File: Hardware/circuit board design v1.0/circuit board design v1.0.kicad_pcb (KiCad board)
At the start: 4 copper layers, 31 x 80 mm, 34 parts, among them IC1 BMI088, J1 Conn_01x06_Male, J3 105017-0001, Q1 2N7002-7-F, U1 STM32F446RETx, U2 W25Q64JVSS, U4 BME280, U5 STF202-22T1G, U6 MAX40203_SOT23, U7 NCP161ASN180T1G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

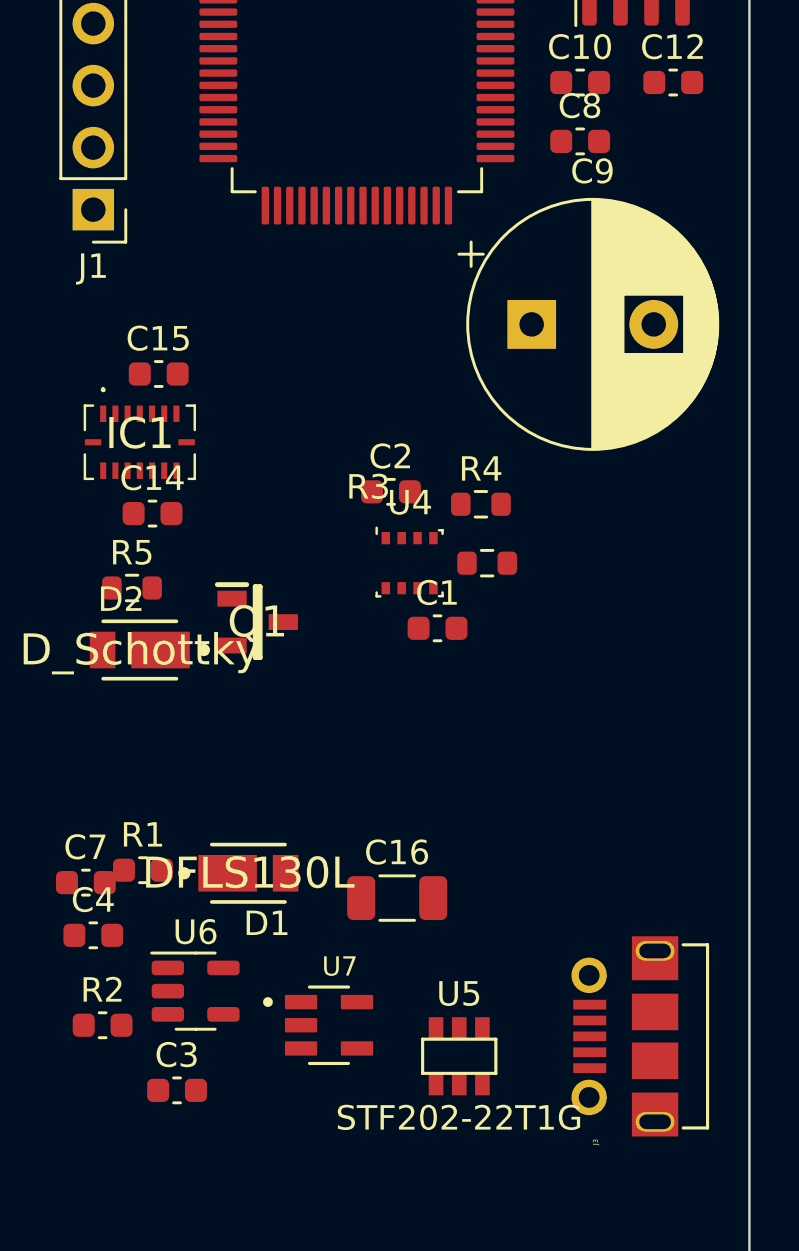
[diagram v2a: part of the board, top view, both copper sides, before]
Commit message: Added spi connection for radio
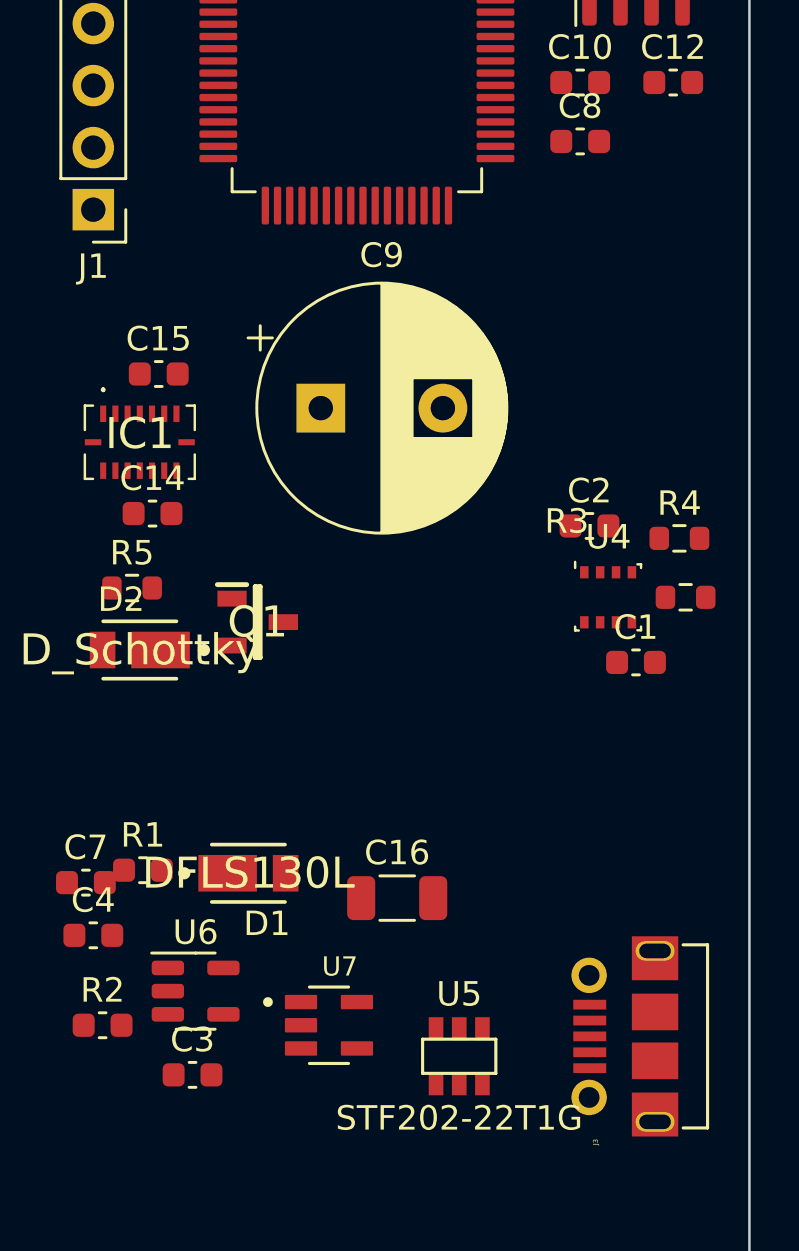
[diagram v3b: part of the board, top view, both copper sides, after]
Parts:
- moved C9 9.29 mm to (33.4, 65.4)
- moved C1 8.25 mm to (46.4, 75.8)
- moved R3 8.25 mm to (48.4, 73.2)
- moved R4 8.25 mm to (48.1, 70.7)
- moved U4 8.25 mm to (45.2, 73.2)
- moved C2 8.25 mm to (44.5, 70.2)
- moved C3 0.90 mm to (28.2, 92.7)
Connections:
- U1 pad 21: unconnected-(U1-Pad21) -> /MCU/SPI1_SCK
- U1 pad 22: unconnected-(U1-Pad22) -> /MCU/SPI1_MISO
- U1 pad 23: unconnected-(U1-Pad23) -> /MCU/SPI1_MOSI
- U1 pad 24: unconnected-(U1-Pad24) -> /MCU/Radio_Enable
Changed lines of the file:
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@@
 (kicad_pcb (version 20211014) (generator pcbnew)
   (general
-    (thickness 4.69)
+    (thickness 1.6062)
   )
   (paper "A4")
@@
       (layer "F.Mask" (type "Top Solder Mask") (thickness 0.01))
       (layer "F.Cu" (type "copper") (thickness 0.035))
-      (layer "dielectric 1" (type "core") (thickness 1.51) (material "FR4") (epsilon_r 4.5) (loss_tangent 0.02))
-      (layer "In1.Cu" (type "copper") (thickness 0.035))
-      (layer "dielectric 2" (type "prepreg") (thickness 1.51) (material "FR4") (epsilon_r 4.5) (loss_tangent 0.02))
-      (layer "In2.Cu" (type "copper") (thickness 0.035))
-      (layer "dielectric 3" (type "core") (thickness 1.51) (material "FR4") (epsilon_r 4.5) (loss_tangent 0.02))
+      (layer "dielectric 1" (type "prepreg") (thickness 0.2104) (material "FR4") (epsilon_r 4.5) (loss_tangent 0.02))
+      (layer "In1.Cu" (type "copper") (thickness 0.0152))
+      (layer "dielectric 2" (type "core") (thickness 1.065) (material "FR4") (epsilon_r 4.5) (loss_tangent 0.02))
+      (layer "In2.Cu" (type "copper") (thickness 0.0152))
+      (layer "dielectric 3" (type "prepreg") (thickness 0.2104) (material "FR4") (epsilon_r 4.5) (loss_tangent 0.02))
       (layer "B.Cu" (type "copper") (thickness 0.035))
       (layer "B.Mask" (type "Bottom Solder Mask") (thickness 0.01))
@@
   (net 18 "unconnected-(IC1-Pad5)")
   (net 19 "unconnected-(U1-Pad20)")
-  (net 20 "unconnected-(U1-Pad21)")
-  (net 21 "unconnected-(U1-Pad22)")
-  (net 22 "unconnected-(U1-Pad23)")
-  (net 23 "unconnected-(U1-Pad24)")
+  (net 20 "/MCU/SPI1_SCK")
+  (net 21 "/MCU/SPI1_MISO")
+  (net 22 "/MCU/SPI1_MOSI")
+  (net 23 "/MCU/Radio_Enable")
   (net 24 "unconnected-(U1-Pad25)")
   (net 25 "unconnected-(U1-Pad26)")
@@
   (net 81 "/MCU/buzzer_gate")
   (footprint "Resistor_SMD:R_0603_1608Metric" (layer "F.Cu")
-    (at 40.005 69.342)
+    (at 48.133 70.739)
     (descr "Resistor SMD 0603 (1608 Metric), square (rectangular) end terminal, IPC_7351 nominal, (Body size source: IPC-SM-782 page 72, https://www.pcb-3d.com/wordpress/wp-content/uploads/ipc-sm-782a_amendment_1_and_2.pdf), generated with kicad-footprint-generator")
     (tags "resistor")
@@
       (effects (font (size 0.200353 0.200353) (thickness 0.15)))
     )
+    (fp_line (start -3.75 2.15) (end 3.75 2.15) (layer "F.SilkS") (width 0.127))
+    (fp_line (start 3.75 1.15) (end 3.75 2.15) (layer "F.SilkS") (width 0.127))
     (fp_line (start -3.75 1.15) (end -3.75 2.15) (layer "F.SilkS") (width 0.127))
-    (fp_line (start 3.75 1.15) (end 3.75 2.15) (layer "F.SilkS") (width 0.127))
-    (fp_line (start -3.75 2.15) (end 3.75 2.15) (layer "F.SilkS") (width 0.127))
-    (fp_line (start 4 -3.6) (end -4 -3.6) (layer "F.CrtYd") (width 0.127))
-    (fp_line (start -4.4 1.7) (end 4.4 1.7) (layer "F.CrtYd") (width 0.127))
-    (fp_line (start -4 -3.6) (end -4 -1.3) (layer "F.CrtYd") (width 0.127))
     (fp_line (start 4.4 1.7) (end 4.4 -1.3) (layer "F.CrtYd") (width 0.127))
-    (fp_line (start -4 -1.3) (end -4.4 -1.3) (layer "F.CrtYd") (width 0.127))
     (fp_line (start -4.4 -1.3) (end -4.4 1.7) (layer "F.CrtYd") (width 0.127))
     (fp_line (start 4.4 -1.3) (end 4 -1.3) (layer "F.CrtYd") (width 0.127))
+    (fp_line (start -4.4 1.7) (end 4.4 1.7) (layer "F.CrtYd") (width 0.127))
+    (fp_line (start -4 -1.3) (end -4.4 -1.3) (layer "F.CrtYd") (width 0.127))
+    (fp_line (start 4 -3.6) (end -4 -3.6) (layer "F.CrtYd") (width 0.127))
+    (fp_line (start -4 -3.6) (end -4 -1.3) (layer "F.CrtYd") (width 0.127))
     (fp_line (start 4 -1.3) (end 4 -3.6) (layer "F.CrtYd") (width 0.127))
     (fp_line (start 4.05 2.55) (end 4.05 2.8) (layer "B.Fab") (width 0.127))
+    (fp_arc (start 4.05 2.8) (mid 3.656711 2.575094) (end 3.5 2.15) (layer "B.Fab") (width 0.127))
     (fp_arc (start 4.05 2.55) (mid 3.824711 2.406466) (end 3.75 2.15) (layer "B.Fab") (width 0.127))
-    (fp_arc (start 4.05 2.8) (mid 3.656711 2.575094) (end 3.5 2.15) (layer "B.Fab") (width 0.127))
-    (fp_line (start 3.75 -2.85) (end -3.75 -2.85) (layer "F.Fab") (width 0.127))
-    (fp_line (start -3.75 -2.85) (end -3.75 2.15) (layer "F.Fab") (width 0.127))
     (fp_line (start -4.7 1.45) (end 4.85 1.45) (layer "F.Fab") (width 0.127))
     (fp_line (start 3.75 2.15) (end 3.75 -2.85) (layer "F.Fab") (width 0.127))
+    (fp_line (start -3.75 -2.85) (end -3.75 2.15) (layer "F.Fab") (width 0.127))
     (fp_line (start -4.05 2.55) (end -4.05 2.8) (layer "F.Fab") (width 0.127))
+    (fp_line (start 3.75 -2.85) (end -3.75 -2.85) (layer "F.Fab") (width 0.127))
+    (fp_arc (start -3.75 2.15) (mid -3.824721 2.406459) (end -4.05 2.55) (layer "F.Fab") (width 0.127))
     (fp_arc (start -3.5 2.15) (mid -3.65671 2.575091) (end -4.05 2.8) (layer "F.Fab") (width 0.127))
-    (fp_arc (start -3.75 2.15) (mid -3.824721 2.406459) (end -4.05 2.55) (layer "F.Fab") (width 0.127))
     (pad "1" smd rect (at -1.3 -2.675 90) (size 0.4 1.35) (layers "F.Cu" "F.Paste" "F.Mask")
       (net 61 "VBUS") (pinfunction "VDD") (pintype "power_in"))
@@
   )
   (footprint "Capacitor_SMD:C_0603_1608Metric" (layer "F.Cu")
-    (at 38.227 74.422)
+    (at 46.355 75.819)
     (descr "Capacitor SMD 0603 (1608 Metric), square (rectangular) end terminal, IPC_7351 nominal, (Body size source: IPC-SM-782 page 76, https://www.pcb-3d.com/wordpress/wp-content/uploads/ipc-sm-782a_amendment_1_and_2.pdf), generated with kicad-footprint-generator")
     (tags "capacitor")
@@
   )
   (footprint "Capacitor_THT:CP_Radial_D10.0mm_P5.00mm" (layer "F.Cu")
-    (at 42.082323 61.976)
+    (at 33.446323 65.405)
     (descr "CP, Radial series, Radial, pin pitch=5.00mm, , diameter=10mm, Electrolytic Capacitor")
     (tags "CP Radial series Radial pin pitch 5.00mm  diameter 10mm Electrolytic Capacitor")
@@
   )
   (footprint "Capacitor_SMD:C_0603_1608Metric" (layer "F.Cu")
-    (at 27.559 93.345)
+    (at 28.194 92.71)
     (descr "Capacitor SMD 0603 (1608 Metric), square (rectangular) end terminal, IPC_7351 nominal, (Body size source: IPC-SM-782 page 76, https://www.pcb-3d.com/wordpress/wp-content/uploads/ipc-sm-782a_amendment_1_and_2.pdf), generated with kicad-footprint-generator")
     (tags "capacitor")
@@
   )
   (footprint "Package_LGA:Bosch_LGA-8_2.5x2.5mm_P0.65mm_ClockwisePinNumbering" (layer "F.Cu")
-    (at 37.084 71.755)
+    (at 45.212 73.152)
     (descr "LGA-8")
     (tags "lga land grid array")
@@
   )
   (footprint "Resistor_SMD:R_0603_1608Metric" (layer "F.Cu")
-    (at 40.259 71.755)
+    (at 48.387 73.152)
     (descr "Resistor SMD 0603 (1608 Metric), square (rectangular) end terminal, IPC_7351 nominal, (Body size source: IPC-SM-782 page 72, https://www.pcb-3d.com/wordpress/wp-content/uploads/ipc-sm-782a_amendment_1_and_2.pdf), generated with kicad-footprint-generator")
     (tags "resistor")
@@
   )
   (footprint "Capacitor_SMD:C_0603_1608Metric" (layer "F.Cu")
-    (at 36.322 68.834)
+    (at 44.45 70.231)
     (descr "Capacitor SMD 0603 (1608 Metric), square (rectangular) end terminal, IPC_7351 nominal, (Body size source: IPC-SM-782 page 76, https://www.pcb-3d.com/wordpress/wp-content/uploads/ipc-sm-782a_amendment_1_and_2.pdf), generated with kicad-footprint-generator")
     (tags "capacitor")
@@
       (net 19 "unconnected-(U1-Pad20)") (pinfunction "PA4") (pintype "bidirectional+no_connect"))
     (pad "21" smd roundrect (at -1.75 5.675) (size 0.3 1.55) (layers "F.Cu" "F.Paste" "F.Mask") (roundrect_rratio 0.25)
-      (net 20 "unconnected-(U1-Pad21)") (pinfunction "PA5") (pintype "bidirectional+no_connect"))
+      (net 20 "/MCU/SPI1_SCK") (pinfunction "PA5") (pintype "bidirectional"))
     (pad "22" smd roundrect (at -1.25 5.675) (size 0.3 1.55) (layers "F.Cu" "F.Paste" "F.Mask") (roundrect_rratio 0.25)
-      (net 21 "unconnected-(U1-Pad22)") (pinfunction "PA6") (pintype "bidirectional+no_connect"))
+      (net 21 "/MCU/SPI1_MISO") (pinfunction "PA6") (pintype "bidirectional"))
     (pad "23" smd roundrect (at -0.75 5.675) (size 0.3 1.55) (layers "F.Cu" "F.Paste" "F.Mask") (roundrect_rratio 0.25)
-      (net 22 "unconnected-(U1-Pad23)") (pinfunction "PA7") (pintype "bidirectional+no_connect"))
+      (net 22 "/MCU/SPI1_MOSI") (pinfunction "PA7") (pintype "bidirectional"))
     (pad "24" smd roundrect (at -0.25 5.675) (size 0.3 1.55) (layers "F.Cu" "F.Paste" "F.Mask") (roundrect_rratio 0.25)
-      (net 23 "unconnected-(U1-Pad24)") (pinfunction "PC4") (pintype "bidirectional+no_connect"))
+      (net 23 "/MCU/Radio_Enable") (pinfunction "PC4") (pintype "bidirectional"))
     (pad "25" smd roundrect (at 0.25 5.675) (size 0.3 1.55) (layers "F.Cu" "F.Paste" "F.Mask") (roundrect_rratio 0.25)
       (net 24 "unconnected-(U1-Pad25)") (pinfunction "PC5") (pintype "bidirectional+no_connect"))

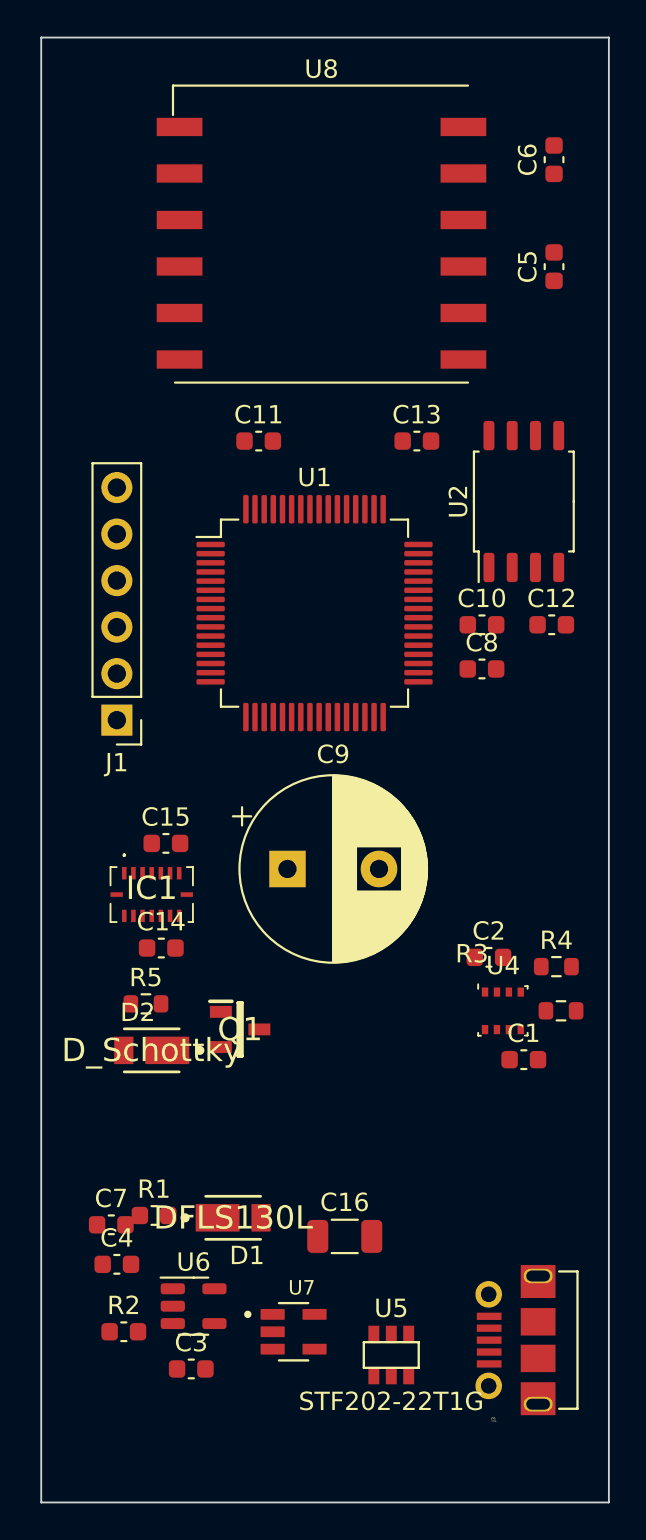
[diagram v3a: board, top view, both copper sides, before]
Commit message: Placed components but not connected yet
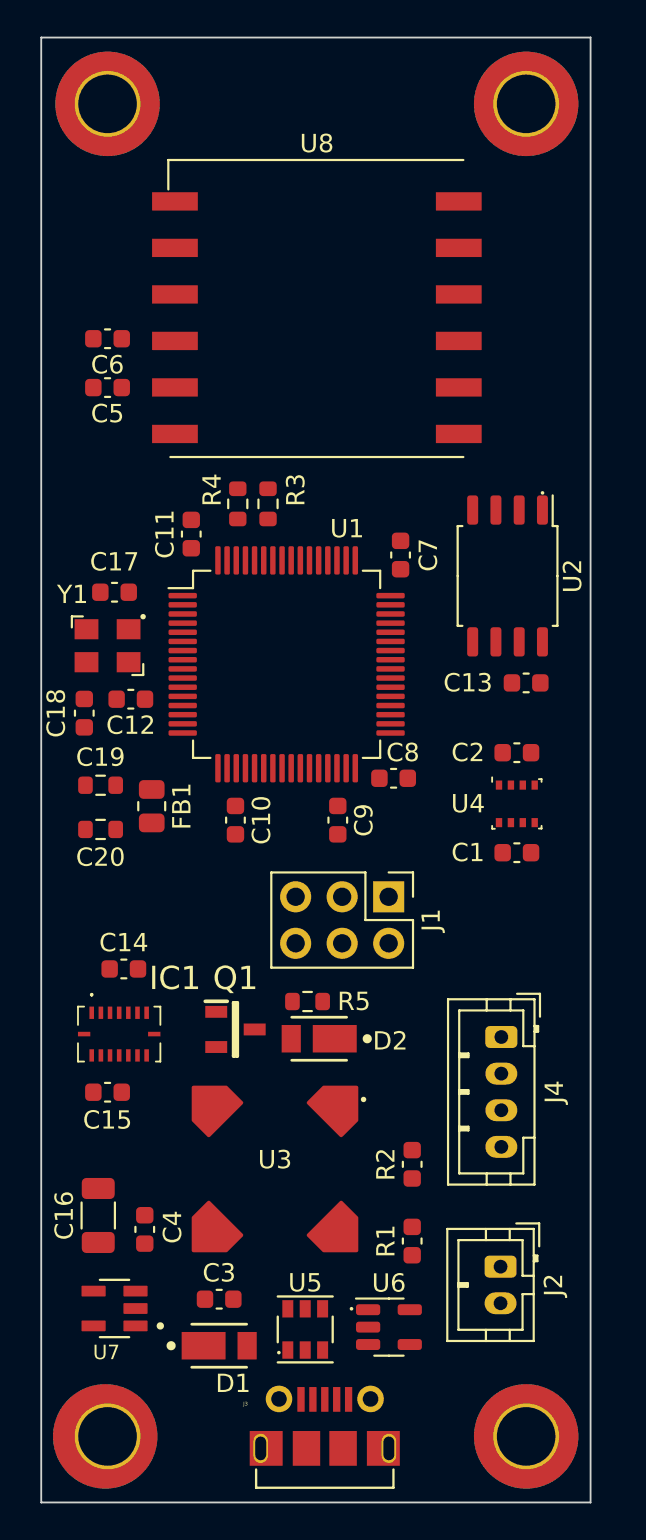
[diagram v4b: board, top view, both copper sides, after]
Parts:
- added C17: 8pF, Capacitor_SMD:C_0603_1608Metric, F.Cu at (24.0, 50.3)
- added C18: 8pF, Capacitor_SMD:C_0603_1608Metric, F.Cu at (22.4, 56.9)
- added C19: 1uF, Resistor_SMD:R_0603_1608Metric, F.Cu at (23.2, 60.8)
- added C20: 1uF, Resistor_SMD:R_0603_1608Metric, F.Cu at (23.2, 63.2)
- added FB1: 120R@100MHz, Resistor_SMD:R_0805_2012Metric, F.Cu at (26.0, 62.0)
- added H1: MountingHole_Pad, MountingHole:MountingHole_3.2mm_M3_ISO7380_Pad_TopBottom, F.Cu at (23.5, 96.4)
- added H2: MountingHole_Pad, MountingHole:MountingHole_3.2mm_M3_ISO7380_Pad_TopBottom, F.Cu at (46.5, 23.6)
- added H3: MountingHole_Pad, MountingHole:MountingHole_3.2mm_M3_ISO7380_Pad_TopBottom, F.Cu at (23.6, 23.6)
- added H4: MountingHole_Pad, MountingHole:MountingHole_3.2mm_M3_ISO7380_Pad_TopBottom, F.Cu at (46.5, 96.4)
- added J2: Conn_01x02, Connector_JST:JST_PH_B2B-PH-K_1x02_P2.00mm_Vertical, F.Cu at (45.1, 87.1)
- added J4: Conn_01x04, Connector_JST:JST_PH_B4B-PH-K_1x04_P2.00mm_Vertical, F.Cu at (45.1, 74.6)
- added U3: SDR08540M3-01, Components:SDR08540M3-01 Buzzer, F.Cu at (32.8, 81.8)
- added Y1: Crystal_GND24, Components:ECS-80-8-33Q-ADS-TR3 Crystal, F.Cu at (23.6, 53.2)
- C1, C2: value 100n -> 100nF
- C14, C15: value C_Small -> 100nF
- C3, C4: value C_Small -> 1uF
- C9: footprint Capacitor_THT:CP_Radial_D10.0mm_P5.00mm -> Capacitor_SMD:C_0603_1608Metric
- J1: footprint Connector_PinHeader_2.54mm:PinHeader_1x06_P2.54mm_Vertical -> Connector_PinHeader_2.54mm:PinHeader_2x03_P2.54mm_Vertical
- R1, R2: value R -> 100k
- moved C7 39.8 mm to (39.6, 48.3), turned to 90 degrees
- moved R3 32.0 mm to (32.4, 45.5), turned to 90 degrees
- moved R4 30.7 mm to (30.7, 45.5), turned to 90 degrees
- moved C6 26.3 mm to (23.6, 36.4), turned to 180 degrees
- moved C5 25.3 mm to (23.6, 39.1), turned to 180 degrees
- moved C12 23.3 mm to (24.9, 56.1), turned to 180 degrees
- moved R2 18.2 mm to (40.3, 81.5), turned to 90 degrees
- moved J1 17.7 mm to (39.0, 66.9), turned to -90 degrees
- moved C10 17.2 mm to (30.6, 62.7), turned to -90 degrees
- moved C13 14.5 mm to (46.5, 55.2), turned to 180 degrees
- moved R1 14.2 mm to (40.3, 85.7), turned to 90 degrees
- moved C15 14.0 mm to (23.6, 77.6)
- moved C16 13.5 mm to (23.1, 84.3), turned to 90 degrees
- moved J3 13.1 mm to (35.5, 97.0), turned to 0 degrees
- moved U4 11.3 mm to (46.0, 61.8)
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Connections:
- IC1 pad 9: /MCU/SCL -> /MCU/SDA
- R1 pad 2: /Power/PWR_BVOLTS -> /MCU/PWR_BVOLTS
- R2 pad 1: /Power/PWR_BVOLTS -> /MCU/PWR_BVOLTS
- R3 pad 1: +3.3V -> /MCU/SDA
- R3 pad 2: /MCU/SCL -> +3.3V
- U1 pad 14: /GPS/rx_gps -> unconnected-(U1-Pad14)
- U1 pad 15: /GPS/tx_gps -> unconnected-(U1-Pad15)
- U1 pad 25: unconnected-(U1-Pad25) -> /MCU/PWR_BVOLTS
- U1 pad 53: unconnected-(U1-Pad53) -> /GPS/rx_gps
- U1 pad 54: unconnected-(U1-Pad54) -> /GPS/tx_gps
- U1 pad 59: /MCU/SCL -> /MCU/SDA
- U4 pad 3: /MCU/SCL -> /MCU/SDA
- U4 pad 6: +3.3V -> unconnected-(U4-Pad6)
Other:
- board size 31 x 80 mm -> 30 x 80 mm

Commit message: Finished routing
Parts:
- J2: footprint Connector_JST:JST_PH_B2B-PH-K_1x02_P2.00mm_Vertical -> Components:JST_PH_B2B-PH-K_1x02_P2.00mm_Vertical
- J4: footprint Connector_JST:JST_PH_B4B-PH-K_1x04_P2.00mm_Vertical -> Components:JST_PH_B4B-PH-K_1x04_P2.00mm_Vertical
- U1: footprint Package_QFP:LQFP-64_10x10mm_P0.5mm -> Components:LQFP-64_10x10mm_P0.5mm
- U2: footprint Package_SO:SOIC-8_5.23x5.23mm_P1.27mm -> Components:W25Q64JVSSIQ
- moved J1 4.41 mm to (41.9, 70.2), turned to 180 degrees
- moved C8 3.24 mm to (36.8, 62.6), turned to -90 degrees
- moved C7 1.17 mm to (40.4, 49.1), turned to 0 degrees
- moved C9 1.02 mm to (35.2, 62.6)
- moved U5 0.92 mm to (34.2, 89.7), turned to 180 degrees
- moved J3 0.51 mm to (35.5, 96.5)
- turned C2 to 180 degrees
- turned C20 to 180 degrees
- turned U6 to 180 degrees
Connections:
- U1 pad 25: /MCU/PWR_BVOLTS -> unconnected-(U1-Pad25)
- U1 pad 27: unconnected-(U1-Pad27) -> /MCU/PWR_BVOLTS
- U3 pad 2: GND -> Net-(D2-Pad2)
- U3 pad 3: GND -> Net-(D2-Pad2)
- U3 pad 4: GND -> Net-(D2-Pad2)
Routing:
- net GND: track 0.00 -> 120.9 mm, vias 0 -> 34
- net +3.3V: track 0.00 -> 77.7 mm, vias 0 -> 22
- net /MCU/SDA: track 0.00 -> 57.0 mm, vias 0 -> 3
- net /MCU/SCL: track 0.00 -> 55.7 mm, vias 0 -> 3
- net +3.3VA: track 0.00 -> 44.3 mm, vias 0 -> 4
- net /MCU/usb_dp: track 0.00 -> 42.7 mm, vias 0 -> 2
- net /MCU/usb_dm: track 0.00 -> 41.8 mm, vias 0 -> 2
- net /MCU/PWR_BVOLTS: track 0.00 -> 33.3 mm, vias 0 -> 2
- net Net-(D2-Pad2): track 0.00 -> 27.0 mm
- net /MCU/SPI1_SCK: track 0.00 -> 26.3 mm
- net /MCU/SPI1_MISO: track 0.00 -> 24.9 mm
- net /MCU/SPI1_MOSI: track 0.00 -> 23.5 mm
- net /GPS/rx_gps: track 0.00 -> 22.9 mm
- net /MCU/Radio_Enable: track 0.00 -> 22.1 mm
- net Net-(C3-Pad1): track 0.00 -> 20.4 mm
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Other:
- board size 30 x 80 mm -> 30 x 79.9 mm
